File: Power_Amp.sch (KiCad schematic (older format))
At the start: 104 parts, among them J10 TEST_1P, J11 TEST_1P, J12 TEST_1P, J13 TEST_1P, J6 TEST_1P, J7 TEST_1P, J8 TEST_1P, J9 TEST_1P, U14 AD8652ARZ, U15 AD8652ARZ, U16 AD8652ARZ, U17 AD8652ARZ

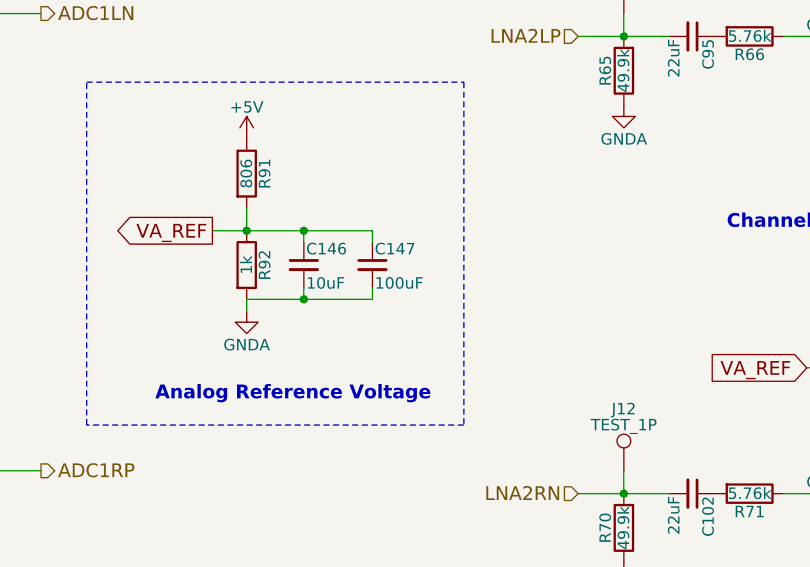
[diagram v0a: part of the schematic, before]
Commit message: change value of C147 capacitor and change some footprint
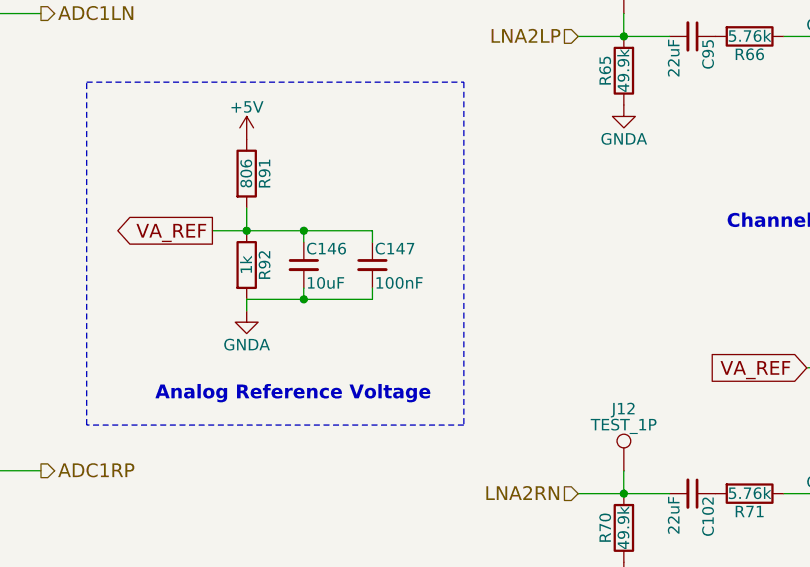
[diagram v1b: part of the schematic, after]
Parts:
- C100, C101, C103, C104, C106, C108, C109, C111, C146, C64, C65, C67, C68, C70, C72, C73, C75, C76, C77, C79, C80, C82, C84, C85, C87, C88, C89, C91, C92, C94, C96, C97, C99: footprint Capacitors_SMD:C_0603 -> Capacitors_SMD:C_0603_HandSoldering
- C102, C105, C107, C110, C66, C69, C71, C74, C78, C81, C83, C86, C90, C93, C95, C98: footprint Capacitors_SMD:C_0603 -> Capacitors_SMD:C_0805_HandSoldering
- C147: value 100uF -> 100nF; footprint Capacitors_SMD:C_0603 -> Capacitors_SMD:C_0603_HandSoldering
